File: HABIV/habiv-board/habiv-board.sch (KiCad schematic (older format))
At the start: 123 parts, among them IC1 RTC_PCF8523T, J1 Micro_SD_Card_Det, J10 Conn_01x02_Female, J11 Conn_01x02_Female, J12 Conn_01x02_Female, J13 Conn_01x02_Female, J14 Conn_01x02_Female, J15 Conn_01x02_Female, J16 Conn_01x02_Female, J17 Conn_01x03_Male, J18 Conn_01x03_Male, J19 Conn_01x03_Male, J2 Conn_ARM_JTAG_SWD_20, J3 Conn_01x02_Male, J4 Conn_01x16_Male, J5 Conn_01x03_Male, J6 Conn_01x16_Male, J7 Conn_01x16_Male, J8 Conn_01x02_Female, J9 Conn_01x02_Male, Q1 32.768KHz, SW1 SW_DPST_x2, U1 STM32F401RET6, U2 MAX31855, U3 FGPMMOPA6H, U4 TPS564208, U5 TPS564208, U6 LSM9DS1TR, U7 MS560702BA03-00, Y1 32.768MHz

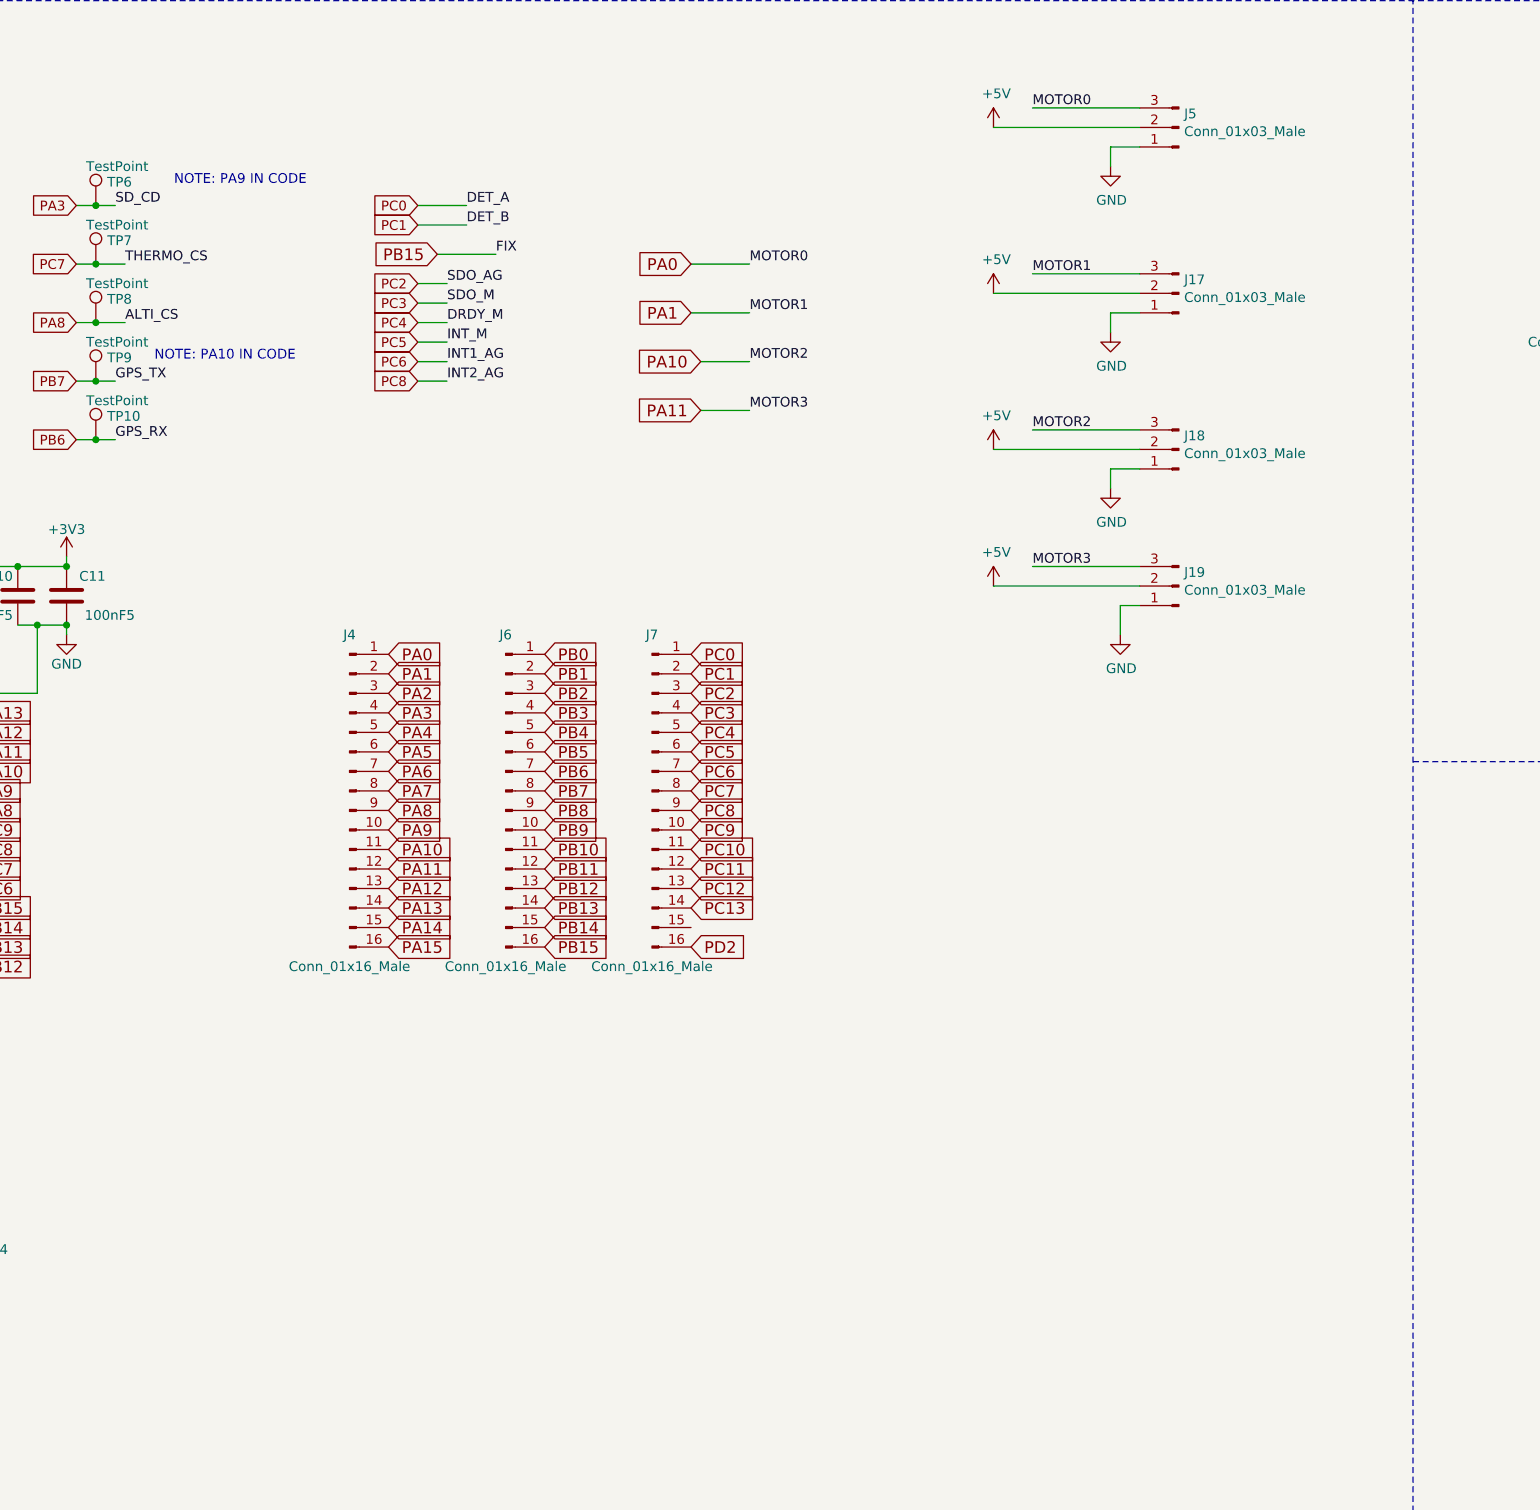
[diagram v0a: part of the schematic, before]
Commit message: add breakouts for rockblock and relay
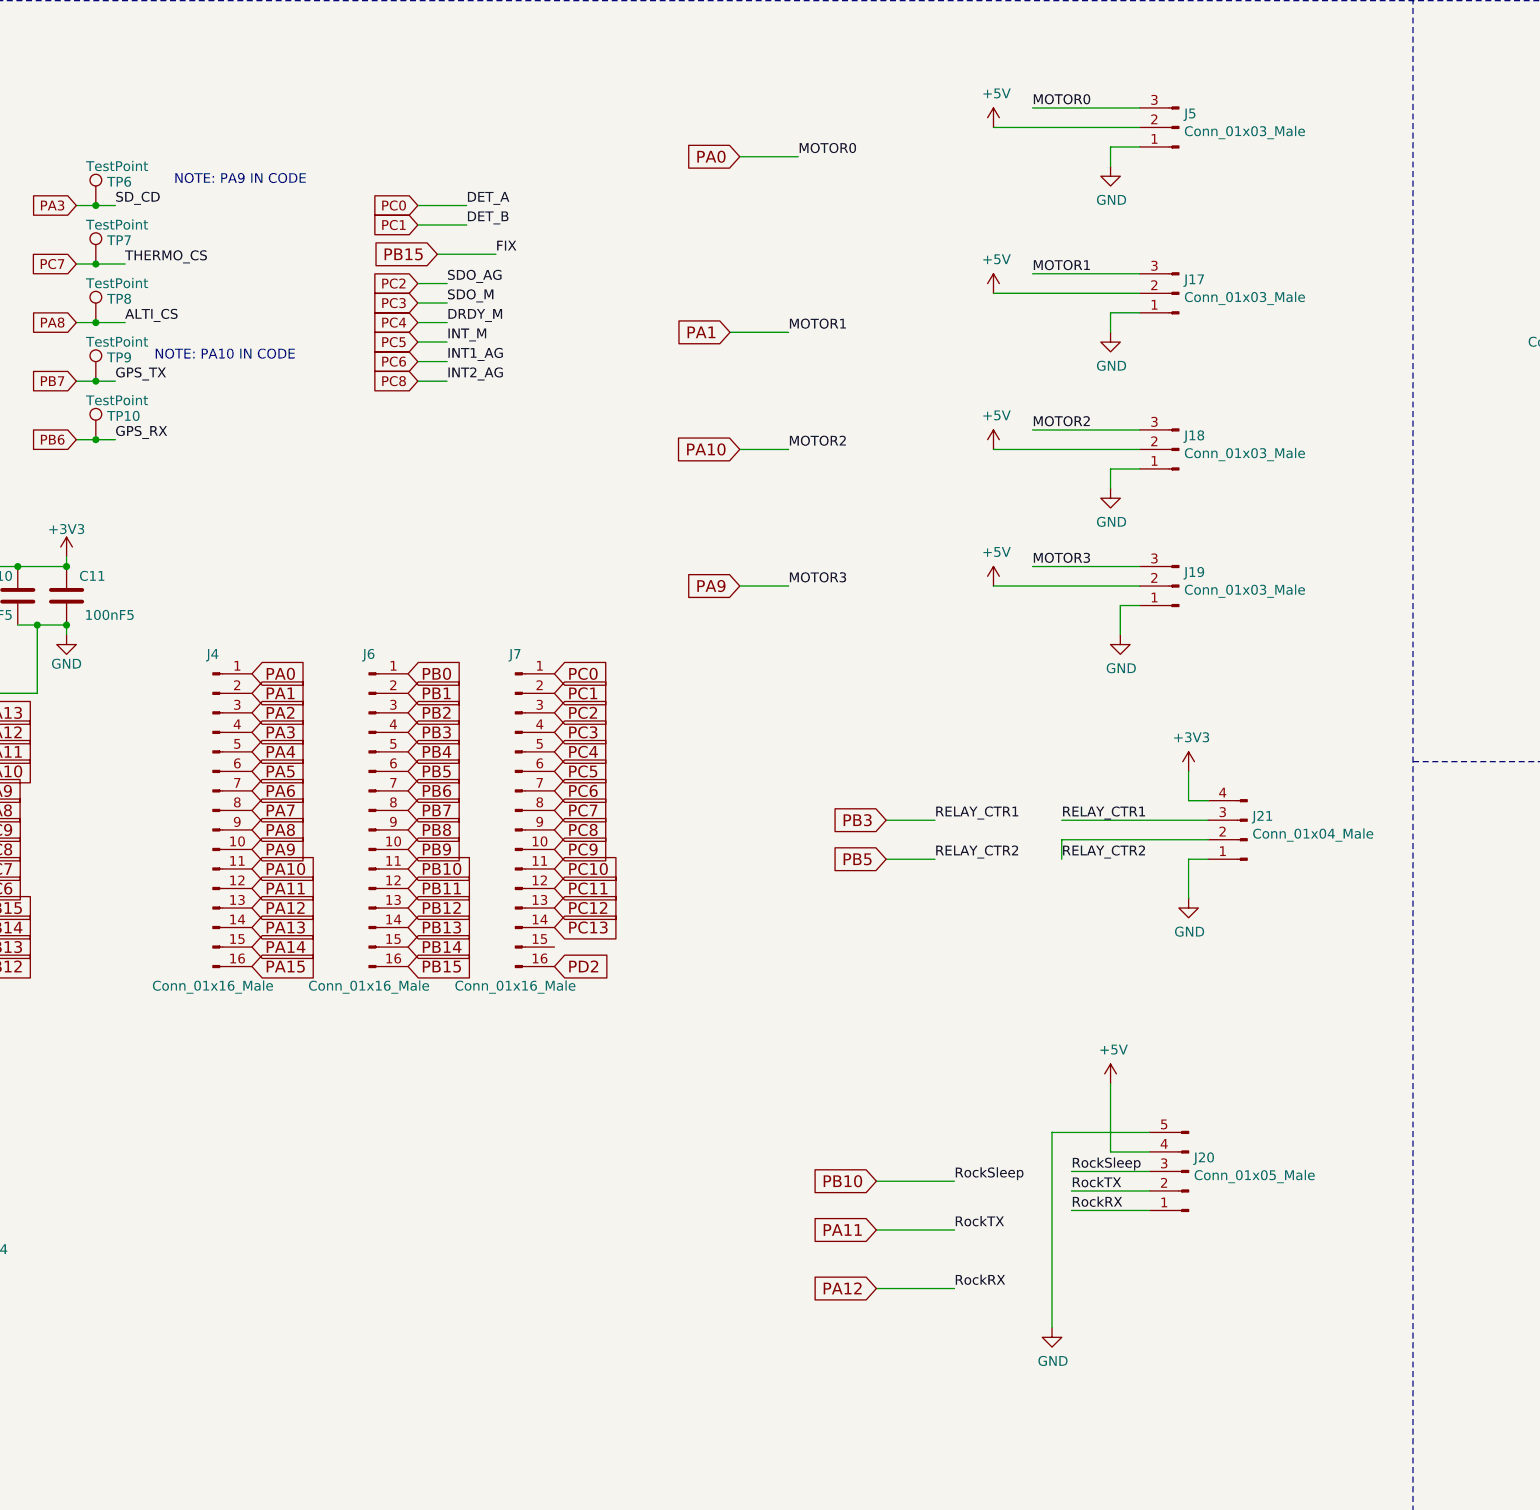
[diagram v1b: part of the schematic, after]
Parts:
- added J20: Conn_01x05_Male, Connector_PinHeader_2.54mm:PinHeader_1x05_P2.54mm_Vertical, symbol Connector:Conn_01x05_Male
- added J21: Conn_01x04_Male, Connector_PinHeader_2.54mm:PinHeader_1x04_P2.54mm_Vertical, symbol Connector:Conn_01x04_Male
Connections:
- net +3V3: now also J21.4 (Pin_4)
- net +5V: now also J20.4 (Pin_4)
- net GND: now also J20.5 (Pin_5), J21.1 (Pin_1)
- net PA11: now also J20.2 (Pin_2); no longer J19.3 (Pin_3)
- net PA12: now also J20.1 (Pin_1)
- net PA9: now also J19.3 (Pin_3)
- net PB10: now also J20.3 (Pin_3)
- net PB3: now also J21.3 (Pin_3)
- net PB5: now also J21.2 (Pin_2)
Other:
- moved on the sheet: J4, J6, J7

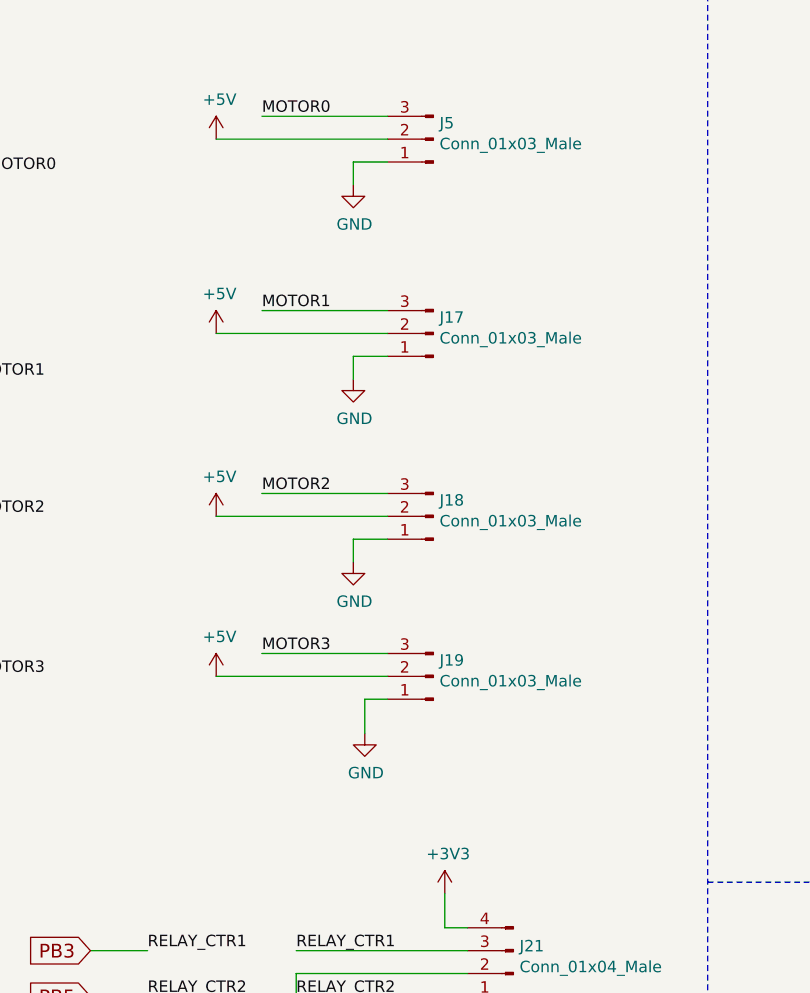
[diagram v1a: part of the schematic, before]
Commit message: add noise reducing caps and fix unconnected in1 plane
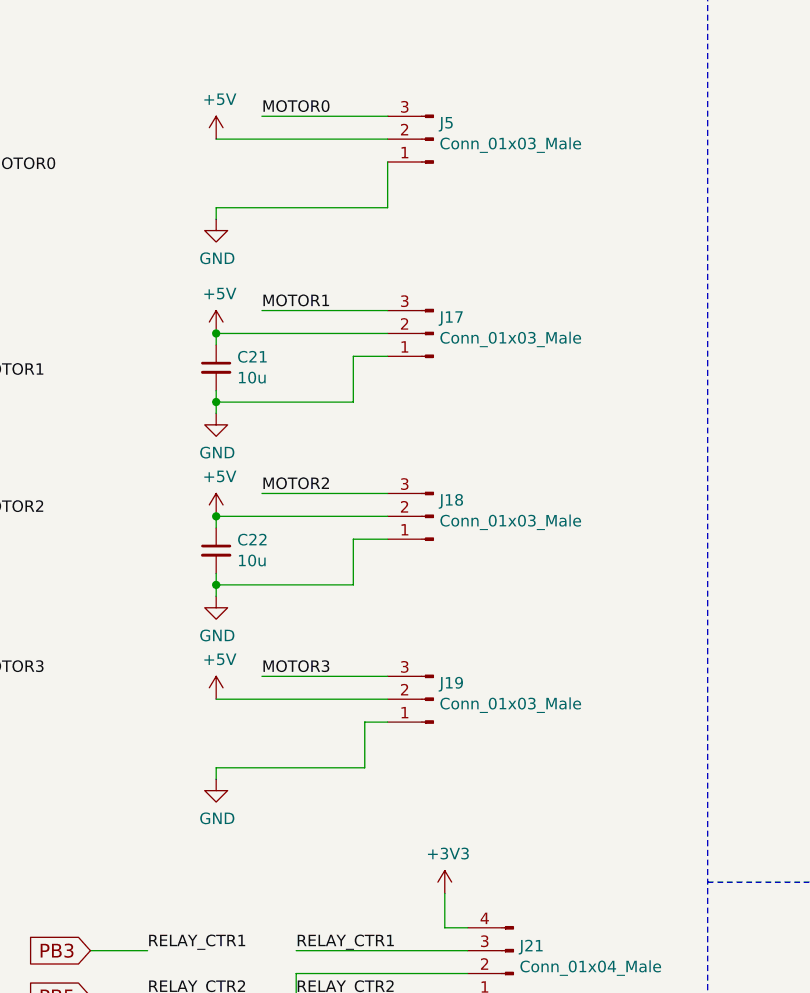
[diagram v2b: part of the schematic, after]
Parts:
- added C21, C22: 10u, Capacitor_SMD:C_0805_2012Metric, symbol Device:C_Small
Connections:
- net +5V: now also C21.1, C22.1
- net GND: now also C21.2, C22.2
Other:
- moved on the sheet: J19
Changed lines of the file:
@@
 L power:GND #PWR0121
 U 1 1 5DFD75A3
-P 12650 5150
-F 0 "#PWR0121" H 12650 4900 50  0001 C CNN
-F 1 "GND" H 12655 4977 50  0000 C CNN
-F 2 "" H 12650 5150 50  0001 C CNN
-F 3 "" H 12650 5150 50  0001 C CNN
-	1    12650 5150
+P 12050 5300
+F 0 "#PWR0121" H 12050 5050 50  0001 C CNN
+F 1 "GND" H 12055 5127 50  0000 C CNN
+F 2 "" H 12050 5300 50  0001 C CNN
+F 3 "" H 12050 5300 50  0001 C CNN
+	1    12050 5300
 	1    0    0    -1
 $EndComp
@@
 Wire Wire Line
 	12650 6700 12800 6700
-Wire Wire Line
-	12650 6800 12650 6700
 $Comp
 L power:GND #PWR0122
 U 1 1 5E012C13
-P 12650 6800
-F 0 "#PWR0122" H 12650 6550 50  0001 C CNN
-F 1 "GND" H 12655 6627 50  0000 C CNN
-F 2 "" H 12650 6800 50  0001 C CNN
-F 3 "" H 12650 6800 50  0001 C CNN
-	1    12650 6800
+P 12050 6950
+F 0 "#PWR0122" H 12050 6700 50  0001 C CNN
+F 1 "GND" H 12055 6777 50  0000 C CNN
+F 2 "" H 12050 6950 50  0001 C CNN
+F 3 "" H 12050 6950 50  0001 C CNN
+	1    12050 6950
 	1    0    0    -1
 $EndComp
 Wire Wire Line
 	12650 5900 12800 5900
-Wire Wire Line
-	12650 6000 12650 5900
 $Comp
 L power:GND #PWR0120
 U 1 1 5DF9A30C
-P 12650 6000
-F 0 "#PWR0120" H 12650 5750 50  0001 C CNN
-F 1 "GND" H 12655 5827 50  0000 C CNN
-F 2 "" H 12650 6000 50  0001 C CNN
-F 3 "" H 12650 6000 50  0001 C CNN
-	1    12650 6000
-	1    0    0    -1
-$EndComp
-Wire Wire Line
-	12700 7400 12800 7400
-Wire Wire Line
-	12700 7550 12700 7400
+P 12050 6150
+F 0 "#PWR0120" H 12050 5900 50  0001 C CNN
+F 1 "GND" H 12055 5977 50  0000 C CNN
+F 2 "" H 12050 6150 50  0001 C CNN
+F 3 "" H 12050 6150 50  0001 C CNN
+	1    12050 6150
+	1    0    0    -1
+$EndComp
+Wire Wire Line
+	12700 7500 12800 7500
 $Comp
 L power:GND #PWR0119
 U 1 1 5DF5FC36
-P 12700 7550
-F 0 "#PWR0119" H 12700 7300 50  0001 C CNN
-F 1 "GND" H 12705 7377 50  0000 C CNN
-F 2 "" H 12700 7550 50  0001 C CNN
-F 3 "" H 12700 7550 50  0001 C CNN
-	1    12700 7550
-	1    0    0    -1
-$EndComp
-Wire Wire Line
-	12050 7300 12800 7300
+P 12050 7750
+F 0 "#PWR0119" H 12050 7500 50  0001 C CNN
+F 1 "GND" H 12055 7577 50  0000 C CNN
+F 2 "" H 12050 7750 50  0001 C CNN
+F 3 "" H 12050 7750 50  0001 C CNN
+	1    12050 7750
+	1    0    0    -1
+$EndComp
+Wire Wire Line
+	12050 7400 12800 7400
 Wire Wire Line
 	12050 6600 12800 6600
@@
 L power:+5V #PWR0118
 U 1 1 5DAFC524
-P 12050 7300
-F 0 "#PWR0118" H 12050 7150 50  0001 C CNN
-F 1 "+5V" H 12065 7473 50  0000 C CNN
-F 2 "" H 12050 7300 50  0001 C CNN
-F 3 "" H 12050 7300 50  0001 C CNN
-	1    12050 7300
+P 12050 7400
+F 0 "#PWR0118" H 12050 7250 50  0001 C CNN
+F 1 "+5V" H 12065 7573 50  0000 C CNN
+F 2 "" H 12050 7400 50  0001 C CNN
+F 3 "" H 12050 7400 50  0001 C CNN
+	1    12050 7400
 	1    0    0    -1
 $EndComp
@@
 $EndComp
 Wire Wire Line
-	12250 7200 12800 7200
+	12250 7300 12800 7300
 Wire Wire Line
 	12250 6500 12800 6500
@@
 L Connector:Conn_01x03_Male J19
 U 1 1 5D268CE1
-P 13000 7300
-F 0 "J19" H 12973 7230 50  0000 R CNN
-F 1 "Conn_01x03_Male" H 12973 7321 50  0000 R CNN
-F 2 "Connector_PinHeader_2.54mm:PinHeader_1x03_P2.54mm_Vertical" H 13000 7300 50  0001 C CNN
-F 3 "~" H 13000 7300 50  0001 C CNN
-	1    13000 7300
+P 13000 7400
+F 0 "J19" H 12973 7330 50  0000 R CNN
+F 1 "Conn_01x03_Male" H 12973 7421 50  0000 R CNN
+F 2 "Connector_PinHeader_2.54mm:PinHeader_1x03_P2.54mm_Vertical" H 13000 7400 50  0001 C CNN
+F 3 "~" H 13000 7400 50  0001 C CNN
+	1    13000 7400
 	-1   0    0    1
 $EndComp
@@
 	-1   0    0    1
 $EndComp
-Text Label 12250 7200 0    50   ~ 0
+Text Label 12250 7300 0    50   ~ 0
 MOTOR3
 Text Label 12250 6500 0    50   ~ 0
@@
 MOTOR1
 Wire Wire Line
-	12650 5050 12800 5050
-Wire Wire Line
-	12650 5150 12650 5050
+	12050 5300 12050 5250
+Wire Wire Line
+	12800 5250 12800 5050
+Wire Wire Line
+	12050 5250 12800 5250
+$Comp
+L Device:C_Small C21
+U 1 1 5D90BE7F
+P 12050 5950
+F 0 "C21" H 12142 5996 50  0000 L CNN
+F 1 "10u" H 12142 5905 50  0000 L CNN
+F 2 "Capacitor_SMD:C_0805_2012Metric" H 12050 5950 50  0001 C CNN
+F 3 "~" H 12050 5950 50  0001 C CNN
+	1    12050 5950
+	1    0    0    -1
+$EndComp
+$Comp
+L Device:C_Small C22
+U 1 1 5D90C077
+P 12050 6750
+F 0 "C22" H 12142 6796 50  0000 L CNN
+F 1 "10u" H 12142 6705 50  0000 L CNN
+F 2 "Capacitor_SMD:C_0805_2012Metric" H 12050 6750 50  0001 C CNN
+F 3 "~" H 12050 6750 50  0001 C CNN
+	1    12050 6750
+	1    0    0    -1
+$EndComp
+Wire Wire Line
+	12050 5800 12050 5850
+Connection ~ 12050 5800
+Wire Wire Line
+	12050 6600 12050 6650
+Connection ~ 12050 6600
+Wire Wire Line
+	12050 6050 12050 6100
+Wire Wire Line
+	12050 6100 12650 6100
+Wire Wire Line
+	12650 5900 12650 6100
+Connection ~ 12050 6100
+Wire Wire Line
+	12050 6100 12050 6150
+Wire Wire Line
+	12050 6850 12050 6900
+Wire Wire Line
+	12050 6900 12650 6900
+Wire Wire Line
+	12650 6700 12650 6900
+Connection ~ 12050 6900
+Wire Wire Line
+	12050 6900 12050 6950
+Wire Wire Line
+	12700 7700 12700 7500
+Wire Wire Line
+	12700 7700 12050 7700
+Wire Wire Line
+	12050 7700 12050 7750
 $EndSCHEMATC

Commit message: renamed some files, updated hab4 code
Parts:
- added R? (x2): 0, symbol Device:R
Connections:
- net +3V3: now also R?.2, R?.2; no longer J1.1 (DAT2), J1.2 (DAT3/CD), J1.3 (CMD), J1.7 (DAT0), J1.8 (DAT1), R13.2, R14.1, R15.2
- new net: J1.1 (DAT2), R?.1
- new net: J1.2 (DAT3/CD), R13.2
- new net: J1.3 (CMD), R15.2
- new net: J1.7 (DAT0), R14.1
- new net: J1.8 (DAT1), R?.1
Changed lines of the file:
@@
 $EndComp
-Wire Wire Line
-	1850 14300 1850 14200
-Wire Wire Line
-	1850 14400 1850 14300
-Connection ~ 1850 14300
 Wire Wire Line
 	2600 14500 1850 14500
 Wire Wire Line
-	1850 14500 1850 14400
-Connection ~ 1850 14400
-Wire Wire Line
-	1850 14800 1850 14500
-Connection ~ 1850 14500
-Wire Wire Line
-	1850 14900 1850 14800
-Connection ~ 1850 14800
-Wire Wire Line
 	2300 15200 2450 15200
 Wire Wire Line
 	2450 15200 2450 15150
-Connection ~ 2450 14800
 Wire Wire Line
 	2450 14800 2600 14800
@@
 Wire Wire Line
 	2550 13800 2550 13950
-Connection ~ 2550 14400
 Wire Wire Line
 	2550 14400 2600 14400
@@
 	1    0    0    -1
 $EndComp
-Connection ~ 1850 14200
 Wire Wire Line
 	5650 13850 5650 13950
@@
 Wire Wire Line
 	2450 14850 2450 14800
-Connection ~ 2450 14300
 Wire Wire Line
 	2450 14300 2600 14300
@@
 SDO
 Wire Wire Line
-	1850 13600 1850 14200
-Wire Wire Line
-	1850 14200 2600 14200
-Wire Wire Line
-	1850 14300 2450 14300
-Wire Wire Line
-	1850 14400 2550 14400
-Wire Wire Line
-	1850 14800 2450 14800
-Wire Wire Line
-	1850 14900 2600 14900
-Wire Wire Line
 	17250 10600 16500 10600
 Wire Wire Line
@@
 Wire Wire Line
 	12050 7700 12050 7750
+Entry Wire Line
+	17750 9250 17850 9350
+Connection ~ 1850 14500
+Wire Wire Line
+	1850 14500 1850 14900
+Wire Wire Line
+	1850 13600 1850 14200
+$Comp
+L Device:R R?
+U 1 1 5DEEF05E
+P 2100 14200
+F 0 "R?" V 2000 14200 50  0000 C CNN
+F 1 "0" V 2100 14200 50  0000 C CNN
+F 2 "" V 2030 14200 50  0001 C CNN
+F 3 "~" H 2100 14200 50  0001 C CNN
+	1    2100 14200
+	0    1    1    0
+$EndComp
+Wire Wire Line
+	1850 14200 1950 14200
+Connection ~ 1850 14200
+Wire Wire Line
+	1850 14200 1850 14500
+Wire Wire Line
+	2250 14200 2600 14200
+$Comp
+L Device:R R?
+U 1 1 5DF70A08
+P 2150 14900
+F 0 "R?" V 2050 14900 50  0000 C CNN
+F 1 "0" V 2150 14900 50  0000 C CNN
+F 2 "" V 2080 14900 50  0001 C CNN
+F 3 "~" H 2150 14900 50  0001 C CNN
+	1    2150 14900
+	0    1    1    0
+$EndComp
+Wire Wire Line
+	1850 14900 2000 14900
+Wire Wire Line
+	2300 14900 2600 14900
 $EndSCHEMATC
